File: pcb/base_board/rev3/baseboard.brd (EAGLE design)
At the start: 88 x 85 mm, 40 parts, among them IC1 LD117AS33TR, P1 RPI3NO-CONNECTORS, SW2 SPST_TACT-EVQQ2, SW5 SPST_TACT-EVQQ2, SW6 SPST_TACT-EVQQ2, SW7 SPST_TACT-EVQQ2, SW8 SPST_TACT-EVQQ2, U5 CH340C

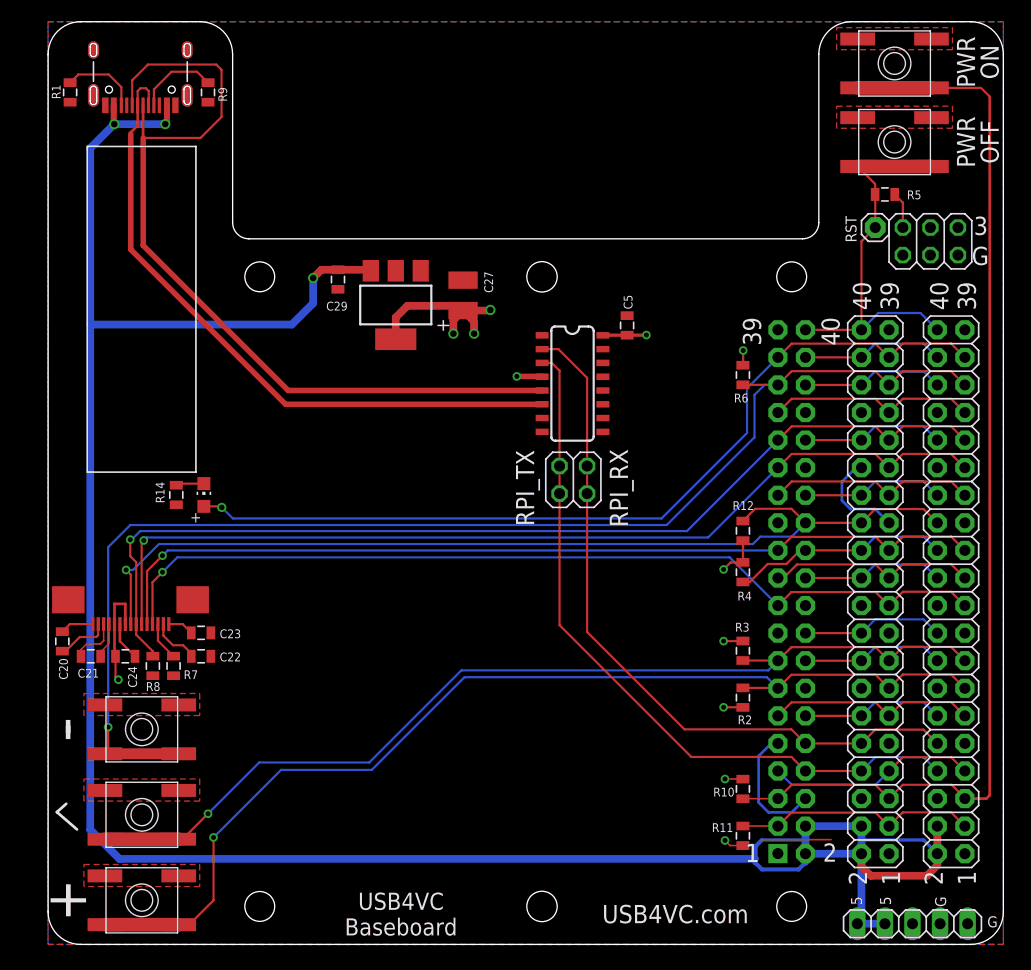
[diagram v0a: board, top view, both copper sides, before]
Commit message: new baseboard revision with more sturdy buttons
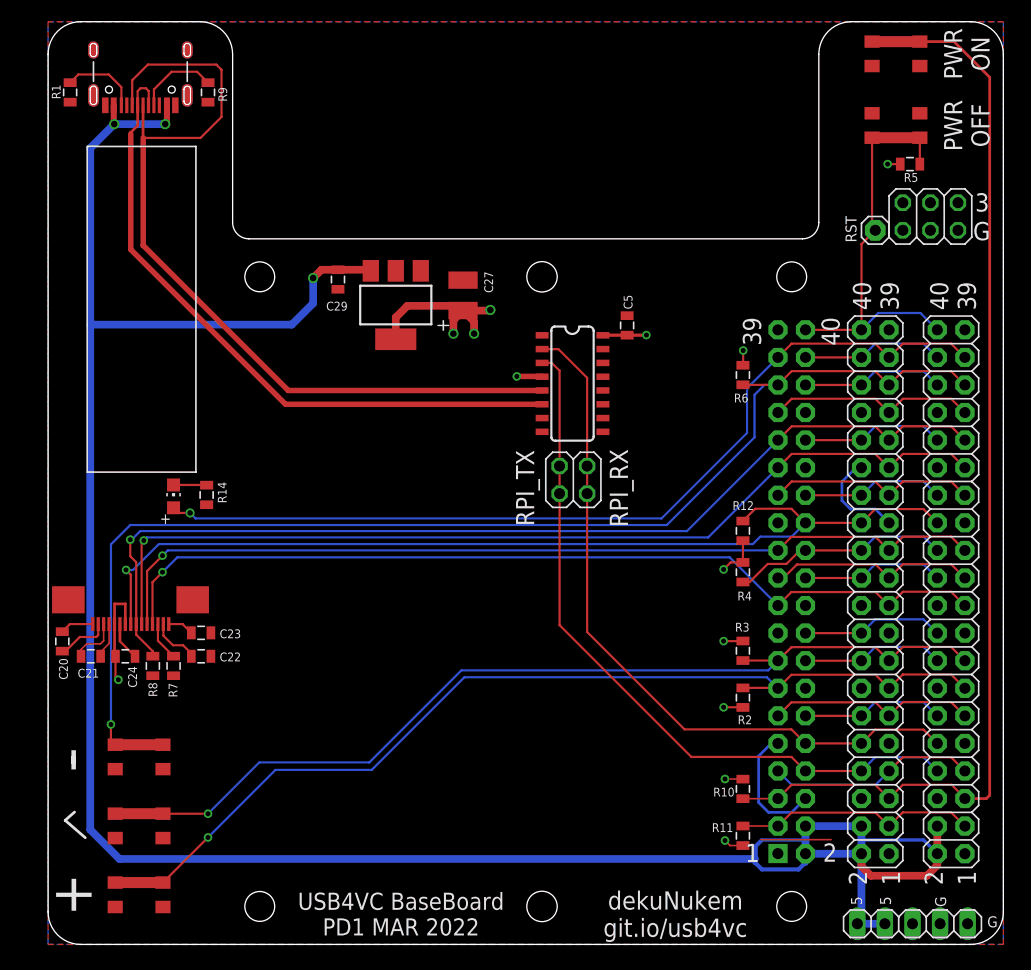
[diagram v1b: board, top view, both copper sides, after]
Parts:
- removed SW5, SW6, SW7, SW8: SPST_TACT-EVQQ2, duckypad:EVQ-Q2
- added SW1, SW20, SW3, SW4: 324_SW, 3pos_slide_switch_centered:342_SWICH_FOOT
- SW2: value SPST_TACT-EVQQ2 -> 324_SW; device duckypad:EVQ-Q2 -> 3pos_slide_switch_centered:342_SWICH_FOOT
- moved SW2 8.13 mm to (78.1, 82.0), turned to 0 degrees
- moved R5 3.63 mm to (79.4, 71.9), turned to 180 degrees
- moved LED1 2.80 mm to (11.6, 41.3)
- moved R14 2.79 mm to (14.6, 41.4)
- moved JP6 2.29 mm to (81.3, 67.1)
- moved JP3 0.25 mm to (76.2, 65.8)
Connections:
- net ENTER_BUTTON: now also SW20.P$2, SW20.P$3; no longer SW6.A, SW6.A'
- net GND: now also SW1.P$1, SW1.P$4, SW2.P$1, SW2.P$4, SW20.P$1, SW20.P$4, SW3.P$1, SW3.P$4, SW4.P$1, SW4.P$4; no longer SW2.A, SW2.A', SW5.B, SW5.B', SW6.B, SW6.B', SW7.B, SW7.B', SW8.B, SW8.B'
- net MINUS_BUTTON: now also SW4.P$2, SW4.P$3; no longer SW5.A, SW5.A'
- net N$32: now also SW3.P$2, SW3.P$3; no longer SW2.B, SW2.B'
- net N$6: now also SW2.P$2, SW2.P$3; no longer SW8.A, SW8.A'
- net PLUS_BUTTON: now also SW1.P$2, SW1.P$3; no longer SW7.A, SW7.A'
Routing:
- net PLUS_BUTTON: track 97.8 -> 91.9 mm
- net MINUS_BUTTON: track 118.9 -> 115.4 mm
- net N$4: track 81.2 -> 84.0 mm
- net +3V3: track 48.6 -> 46.4 mm, vias 12 -> 13
- net N$32: track 36.5 -> 38.6 mm
- net ENTER_BUTTON: track 91.3 -> 89.6 mm
- net N$6: track 101.9 -> 103.3 mm
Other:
- board text added: "USB4VC BaseBoard PD1 MAR 2022"
- board text added: "dekuNukem git.io/usb4vc"
- board text removed: "USB4VC Baseboard"
- board text removed: "USB4VC.com"
